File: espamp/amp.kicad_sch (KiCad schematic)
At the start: 1 part, among them U501 TAS5825MRHB

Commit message: amp schematic draft
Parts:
- added C501, C502: 22uF, Capacitor_SMD:C_Elec_5x5.8, symbol Device:C_Polarized
- added C503, C505, C506: 1uF, Capacitor_SMD:C_0603_1608Metric, symbol Device:C
- added C504, C507: 100nF, Capacitor_SMD:C_0603_1608Metric, symbol Device:C
- added C508: 4.7uF, Capacitor_SMD:C_0603_1608Metric, symbol Device:C
- added C509, C510, C511, C512: 470nF, Capacitor_SMD:C_0603_1608Metric, symbol Device:C
- added C513, C514, C515, C516: 680nF, Capacitor_SMD:C_0603_1608Metric, symbol Device:C
- added H501, H502, H503, H504: MountingHole_Pad, MountingHole:MountingHole_4mm_Pad_Via, symbol Mechanical:MountingHole_Pad
- added L501, L502, L503, L504: SL1040-100M, easyeda2kicad:IND-SMD_L11.0-W10.2, symbol easyeda2kicad:SL1040-100M
- added R501: 0, Resistor_SMD:R_0603_1608Metric, symbol Device:R
- added R502, R503, R504, R505: 10k, Resistor_SMD:R_0603_1608Metric, symbol Device:R
- added TP501, TP502, TP503, TP504: TestPoint, Connector_PinHeader_1.00mm:PinHeader_1x01_P1.00mm_Vertical, symbol Connector:TestPoint
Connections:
- net at U501.1 (BST_A+): now also C510.1
- net at U501.10 (GPIO1): now also R502.2, TP503.1
- net at U501.11 (GPIO2): now also R504.2, TP504.1
- net I2S.LRCLK: now reaches U501.12 (LRCLK)
- net I2S.SCLK: now reaches U501.13 (SCLK)
- net I2S.SDIN: now reaches U501.14 (SDIN)
- net I2C.SDA: now reaches U501.15 (SDA)
- net I2C.SCL: now reaches U501.16 (SCL)
- net at U501.17 (~{PDN}): now also R505.2, TP501.1
- net at U501.18 (GVDD): now also C503.1
- net at U501.19 (AVDD): now also C506.1
- net at U501.2 (OUT_A+): now also C510.2, L501.1
- net GND: now reaches U501.20 (AGND)
- net GND: now also U501.25 (PGND), U501.26 (PGND), U501.31 (PGND), U501.32 (PGND), U501.33 (EP), U501.5 (DGND), C501.2, C502.2, C503.2, C504.2, C505.2, C506.2, C507.2, C508.2, C513.2, C514.2, C515.2, C516.2, R501.2
- net 20V: now reaches U501.21 (PVDD), U501.22 (PVDD), U501.3 (PVDD), U501.4 (PVDD)
- net 20V: now also C501.1, C502.1, C504.1
- net at U501.23 (OUT_B+): now also C511.2, L503.1
- net at U501.24 (BST_B+): now also C511.1
- net at U501.27 (OUT_B-): now also C512.2, L504.1
- net at U501.28 (BST_B-): now also C512.1
- net at U501.29 (BST_A-): now also C509.1
- net at U501.30 (OUT_A-): now also C509.2, L502.1
- net 3V3: now reaches U501.6 (DVDD)
- net 3V3: now also C507.1, C508.1, R502.1, R503.1, R504.1, R505.1
- net at U501.7 (VR_DIG): now also C505.1
- net at U501.8 (ADR): now also R501.1
- net at U501.9 (GPIO0): now also R503.2, TP502.1
- new net: C516.1, H504.1, L504.2
- new net: C513.1, H501.1, L501.2
- new net: C514.1, H502.1, L502.2
- new net: C515.1, H503.1, L503.2

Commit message: tweaks
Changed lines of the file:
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@@
 	)
 	(junction
-		(at 177.8 35.56)
+		(at 158.75 52.07)
 		(diameter 0)
 		(color 0 0 0 0)
@@
 	)
 	(junction
+		(at 177.8 35.56)
+		(diameter 0)
+		(color 0 0 0 0)
+	)
+	(junction
 		(at 59.69 57.15)
 		(diameter 0)
@@
 	(wire
 		(pts
+			(xy 177.8 52.07) (xy 158.75 52.07)
+		)
+		(stroke
+			(width 0)
+			(type default)
+		)
+	)
+	(wire
+		(pts
 			(xy 170.18 85.09) (xy 185.42 85.09)
 		)
@@
 	(wire
 		(pts
+			(xy 177.8 35.56) (xy 177.8 52.07)
+		)
+		(stroke
+			(width 0)
+			(type default)
+		)
+	)
+	(wire
+		(pts
 			(xy 138.43 105.41) (xy 138.43 110.49)
 		)
@@
 					(unit 1)
 				)
-			)
-		)
-	)
-	(symbol
-		(lib_id "power:GND")
-		(at 177.8 35.56 0)
-		(unit 1)
-		(exclude_from_sim no)
-		(in_bom yes)
-		(on_board yes)
-		(dnp no)
-		(fields_autoplaced yes)
-		(property "Reference" "#PWR0503"
-			(at 177.8 41.91 0)
-			(effects
-				(font
-					(size 1.27 1.27)
-				)
-				(hide yes)
-			)
-		)
-		(property "Value" "GND"
-			(at 177.8 40.64 0)
-			(effects
-				(font
-					(size 1.27 1.27)
-				)
-			)
-		)
-		(property "Footprint" ""
-			(at 177.8 35.56 0)
-			(effects
-				(font
-					(size 1.27 1.27)
-				)
-				(hide yes)
-			)
-		)
-		(property "Datasheet" ""
-			(at 177.8 35.56 0)
-			(effects
-				(font
-					(size 1.27 1.27)
-				)
-				(hide yes)
-			)
-		)
-		(property "Description" "Power symbol creates a global label with name \"GND\" , ground"
-			(at 177.8 35.56 0)
-			(effects
-				(font
-					(size 1.27 1.27)
-				)
-				(hide yes)
-			)
-		)
-		(pin "1"
-		)
-		(instances
-			(project "espamp"
-				(path "/48ddfdd8-68fa-4e63-aa18-bc113cdf8cfa/6d838d19-4ba8-44ad-a949-ec7e36a56135"
-					(reference "#PWR0503")
-					(unit 1)
-				)

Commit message: first draft of amp layout
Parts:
- removed C509, C510, C511, C512: 470nF, Capacitor_SMD:C_0603_1608Metric, symbol Device:C
- removed C513, C514, C515, C516: 680nF, Capacitor_SMD:C_0603_1608Metric, symbol Device:C
- added C509, C510, C511, C520: MPP474J2A0701, easyeda2kicad:CAP-TH_L9.5-W3.7-P7.50-D0.5, symbol easyeda2kicad:MPP474J2A0701
- added C517: 100nF, Capacitor_SMD:C_0603_1608Metric, symbol Device:C
- added C518, C519: 22uF, Capacitor_SMD:C_Elec_5x5.8, symbol Device:C_Polarized
- added U502, U503, U504, U505: MPP684J2S1001, easyeda2kicad:CAP-TH_L12.0-W5.8-P10.00-D0.6, symbol easyeda2kicad:MPP684J2S1001
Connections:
- net 20V: now also C517.1, C518.1, C519.1
- net GND: now also C517.2, C518.2, C519.2, U502.1, U503.1, U504.1, U505.1
- net OUT_B-: now reaches L504.1, U501.27 (OUT_B-)
- net OUT_B-: now also C520.2
- net B-: now reaches H504.1, L504.2
- net B-: now also U505.2
- net BST_B+: now reaches U501.24 (BST_B+)
- net BST_B+: now also C509.1
- net OUT_B+: now reaches L503.1, U501.23 (OUT_B+)
- net OUT_B+: now also C509.2
- net A+: now reaches H501.1, L501.2
- net A+: now also U502.2
- net OUT_A-: now reaches L502.1, U501.30 (OUT_A-)
- net OUT_A-: now also C510.2
- net A-: now reaches H502.1, L502.2
- net A-: now also U503.2
- net B+: now reaches H503.1, L503.2
- net B+: now also U504.2
- net BST_A-: now reaches U501.29 (BST_A-)
- net BST_A-: now also C510.1
- net OUT_A+: now reaches L501.1, U501.2 (OUT_A+)
- net OUT_A+: now also C511.2
- net BST_B-: now reaches U501.28 (BST_B-)
- net BST_B-: now also C520.1
- net BST_A+: now reaches U501.1 (BST_A+)
- net BST_A+: now also C511.1
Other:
- moved on the sheet: H501, H502, H503, H504

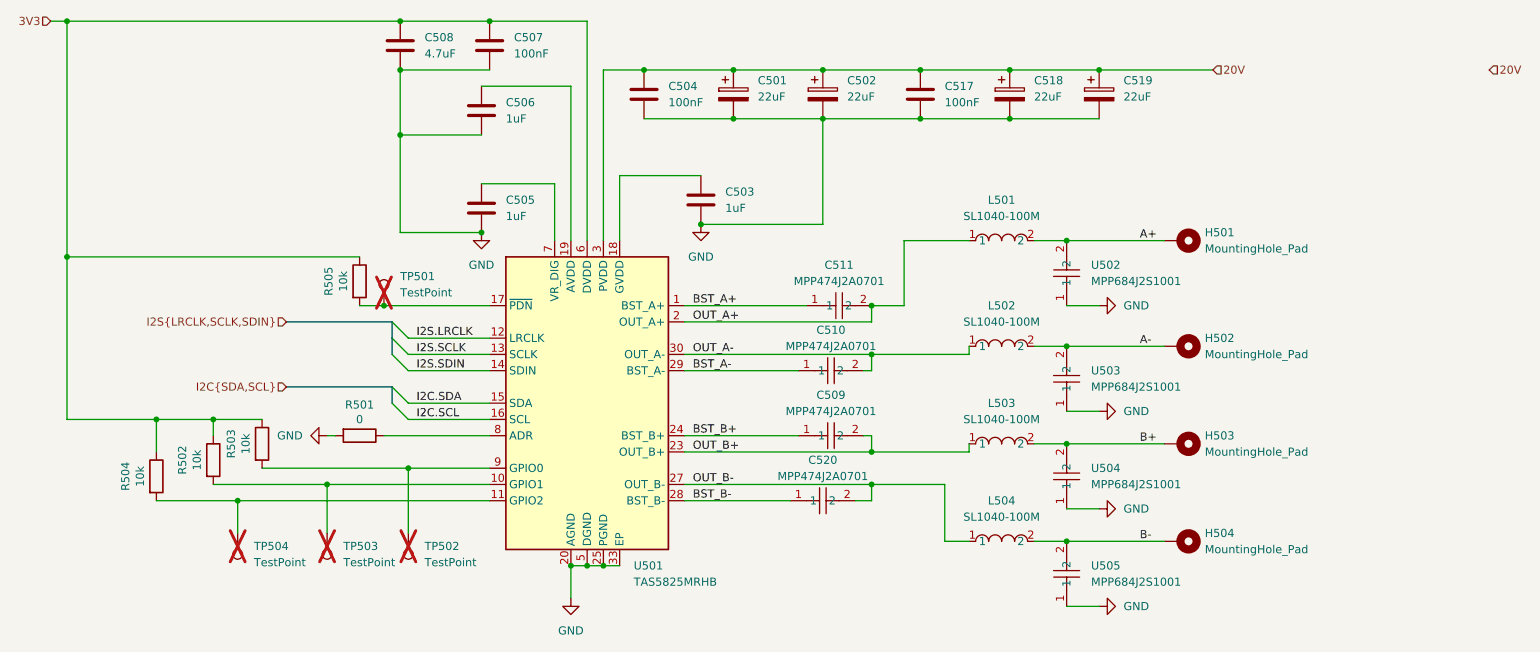
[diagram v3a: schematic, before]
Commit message: amp schematic complete
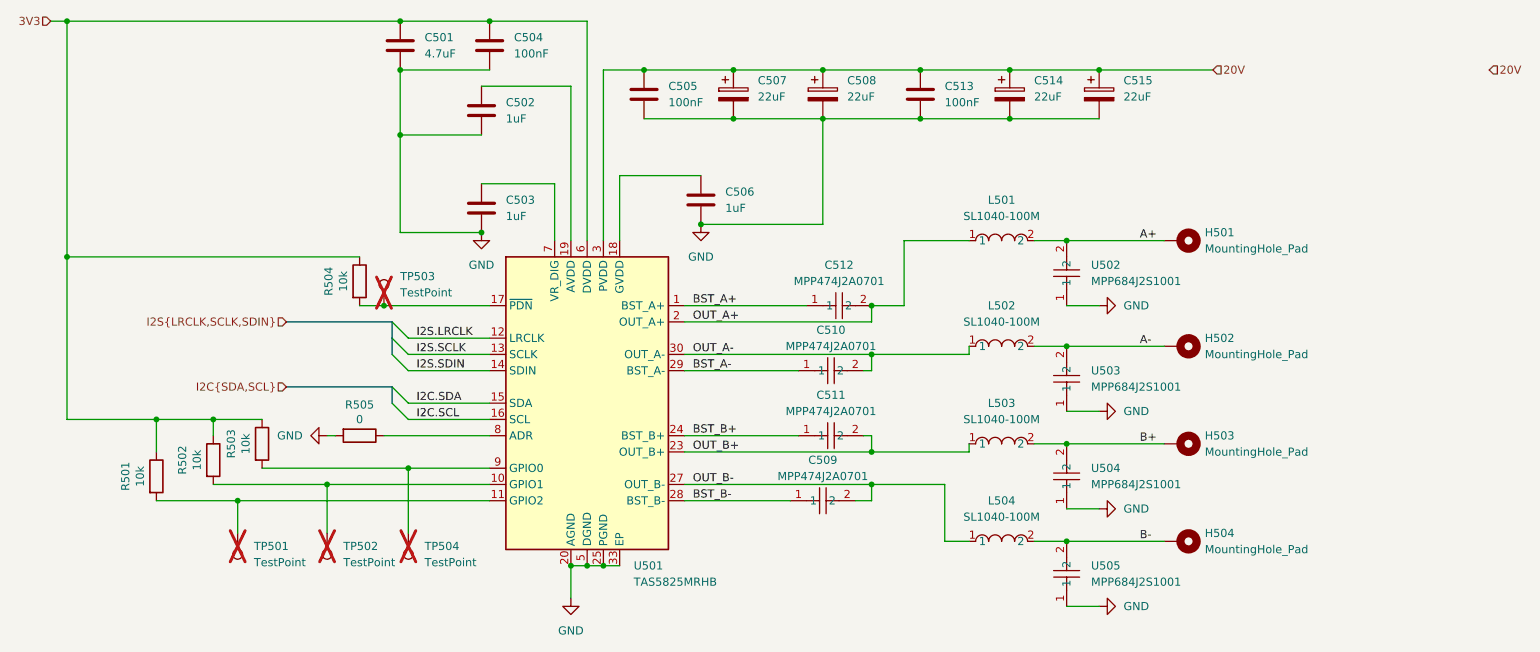
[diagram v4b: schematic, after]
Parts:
- renumbered C508 to C501, C506 to C502, C505 to C503, C507 to C504, C504 to C505, C503 to C506, C501 to C507, C502 to C508, C520 to C509, C509 to C511, C511 to C512, C517 to C513, C518 to C514, C519 to C515, R504 to R501, R505 to R504, R501 to R505, TP504 to TP501, TP503 to TP502, TP501 to TP503, TP502 to TP504

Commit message: espamp revisions
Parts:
- removed TP501, TP502, TP503, TP504: TestPoint, Connector_PinHeader_1.00mm:PinHeader_1x01_P1.00mm_Vertical, symbol Connector:TestPoint
- added C516: 1uF, Capacitor_SMD:C_0603_1608Metric, symbol Device:C
- added TP501, TP502, TP503, TP504, TP505, TP506, TP507, TP508, TP509: LabeledTestPoint, easyeda2kicad:LabeledTestPoint, symbol easyeda2kicad:LabeledTestPoint
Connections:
- net GND: now also C516.1
- net I2C.SCL: now also TP508.1
- net I2C.SDA: now also TP507.1
- net I2S.LRCLK: now also TP504.1
- net I2S.SCLK: now also TP505.1
- net I2S.SDIN: now also TP506.1
- net GPIO2: now reaches R501.2, U501.11 (GPIO2)
- net GPIO2: now also TP501.1
- net GPIO0: now reaches R503.2, U501.9 (GPIO0)
- net GPIO0: now also TP503.1
- net GPIO1: now reaches R502.2, U501.10 (GPIO1)
- net GPIO1: now also TP502.1
- net PDN: now reaches R504.2, U501.17 (~{PDN})
- net PDN: now also C516.2, TP509.1
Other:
- moved on the sheet: R504
